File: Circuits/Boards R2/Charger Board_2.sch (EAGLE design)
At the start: 100 parts, among them CON1 ISP(2X3), CON10 HEADER_3X1, CON11 HEADER_3X1, CON12 HEADER_3X1, CON13 HEADER_4X1, CON14 HEADER_3X1, CON15 HEADER_3X1, CON16 HEADER_4X1, CON17 HEADER_3X1, CON18 HEADER_3X1, CON2 SCREWTERMINAL_1X2, CON3 HEADER_3X1, CON4 HEADER_3X1, CON5 HEADER_3X1, CON6 HEADER_3X1, CON7 HEADER_3X1, CON8 HEADER_3X1, CON9 HEADER_3X1, IC1 NCP1117DT33G, T1 NPN2N2222, T2 NPN2N2222, T3 SI4421DY, T4 MMSS8550-L, T5 MMSS8550-L, T6 MMSS8550-L, U1 ATMEGA324P, U2 ACS711, U3 JOYSTICKPTH, U4 MX25L25735E

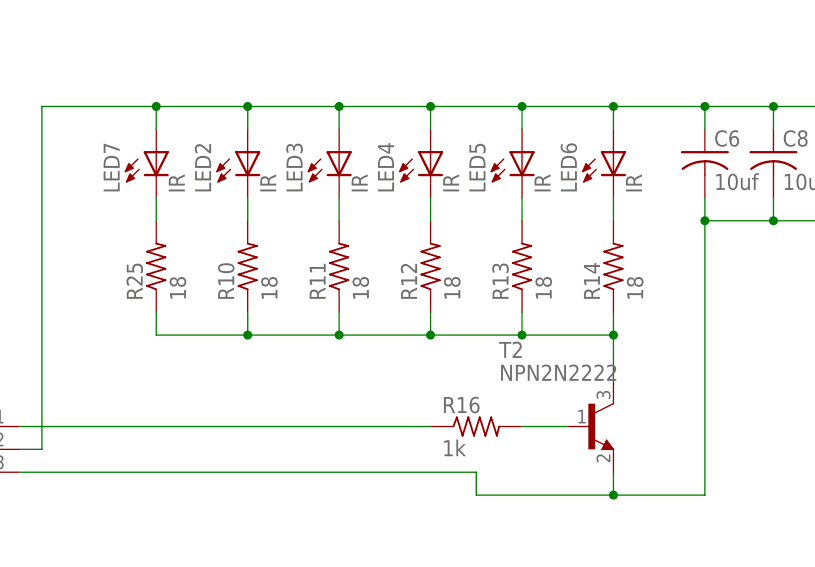
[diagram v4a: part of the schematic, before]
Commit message: slight updates to part values to account for availibility
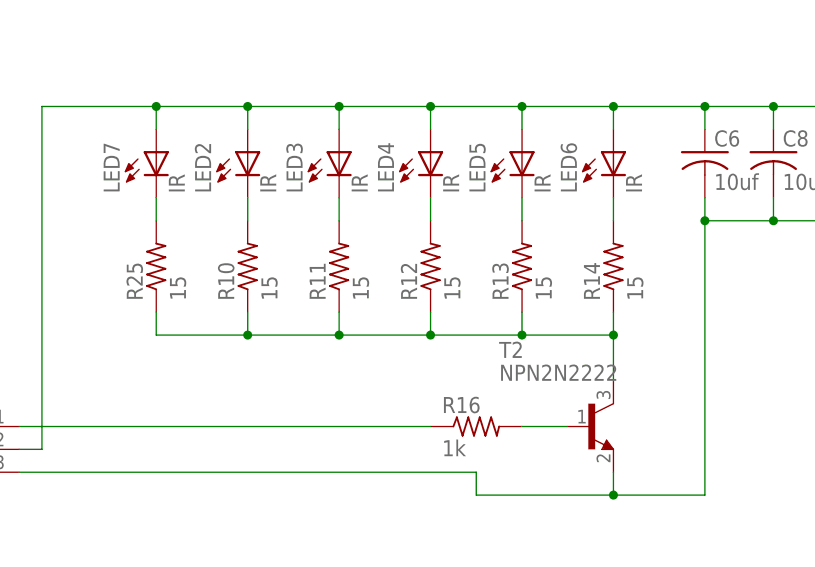
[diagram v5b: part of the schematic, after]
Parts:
- R10, R11, R12, R13, R14, R25: value 18 -> 15
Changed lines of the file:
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@@
 <?xml version="1.0" encoding="utf-8"?>
 <!DOCTYPE eagle SYSTEM "eagle.dtd">
-<eagle version="6.3">
+<eagle version="6.2">
 <drawing>
 <settings>
@@
 <part name="T1" library="Passive" deviceset="NPN2N2222" device=""/>
 <part name="T2" library="Passive" deviceset="NPN2N2222" device=""/>
-<part name="R10" library="Passive" deviceset="RES" device="0603" value="18"/>
-<part name="R11" library="Passive" deviceset="RES" device="0603" value="18"/>
-<part name="R12" library="Passive" deviceset="RES" device="0603" value="18"/>
-<part name="R13" library="Passive" deviceset="RES" device="0603" value="18"/>
-<part name="R14" library="Passive" deviceset="RES" device="0603" value="18"/>
+<part name="R10" library="Passive" deviceset="RES" device="0603" value="15"/>
+<part name="R11" library="Passive" deviceset="RES" device="0603" value="15"/>
+<part name="R12" library="Passive" deviceset="RES" device="0603" value="15"/>
+<part name="R13" library="Passive" deviceset="RES" device="0603" value="15"/>
+<part name="R14" library="Passive" deviceset="RES" device="0603" value="15"/>
 <part name="R16" library="Passive" deviceset="RES" device="0603" value="1k"/>
 <part name="LED2" library="Passive" deviceset="LED" device="5MMRA" value="IR"/>
@@
 <part name="+3V12" library="Supply" deviceset="+3V3" device=""/>
 <part name="LED7" library="Passive" deviceset="LED" device="5MMRA" value="IR"/>
-<part name="R25" library="Passive" deviceset="RES" device="0603" value="18"/>
+<part name="R25" library="Passive" deviceset="RES" device="0603" value="15"/>
 <part name="H5" library="Mechanical" deviceset="MOUNTINGHOLE" device=""/>
 <part name="H6" library="Mechanical" deviceset="MOUNTINGHOLE" device=""/>
